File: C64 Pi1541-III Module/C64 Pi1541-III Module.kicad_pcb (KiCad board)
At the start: 2 copper layers, 100 x 100 mm, 25 parts, among them J1 DC IN, J2 C64_IEC, J3 C64_IEC, J8 Module_Panel, M1 Mounting, M2 Mounting, M3 Mounting, M4 Mounting, U1 7406

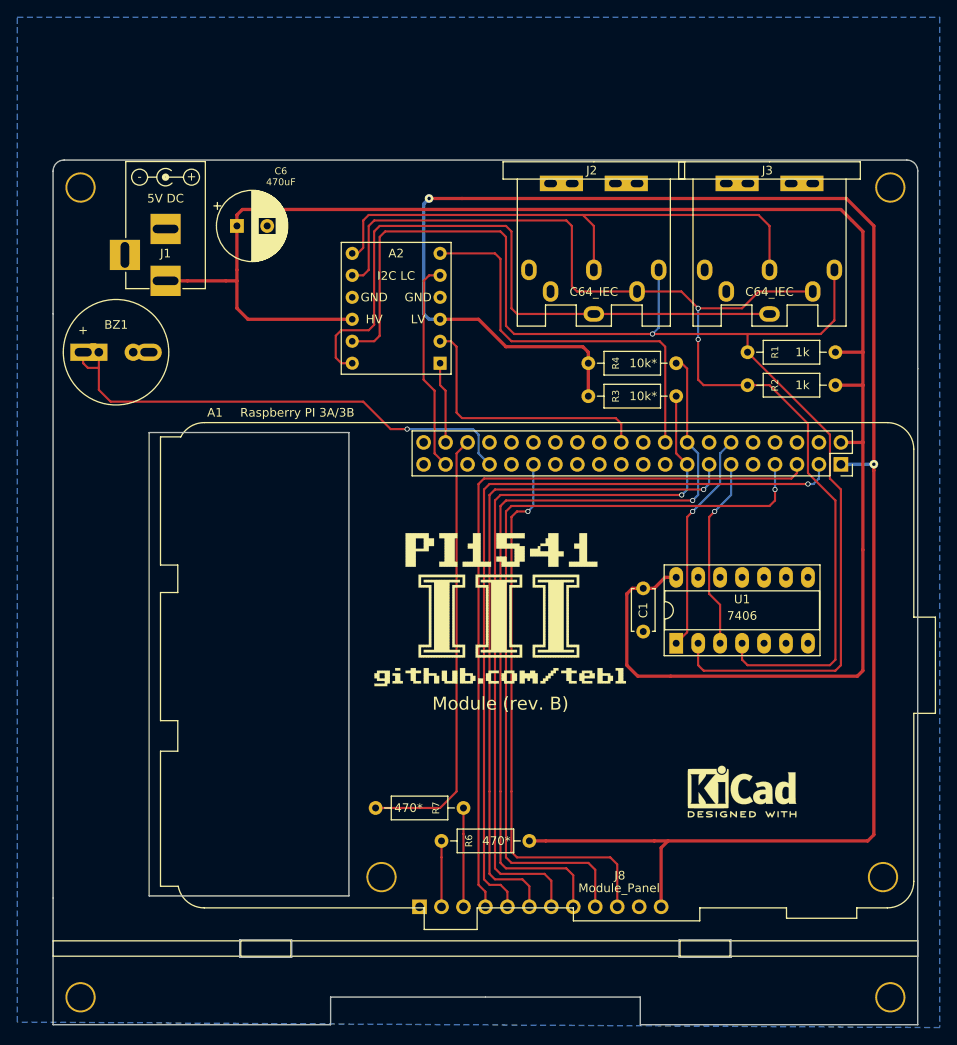
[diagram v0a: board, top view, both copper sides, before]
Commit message: Moved components around to make it easier to build
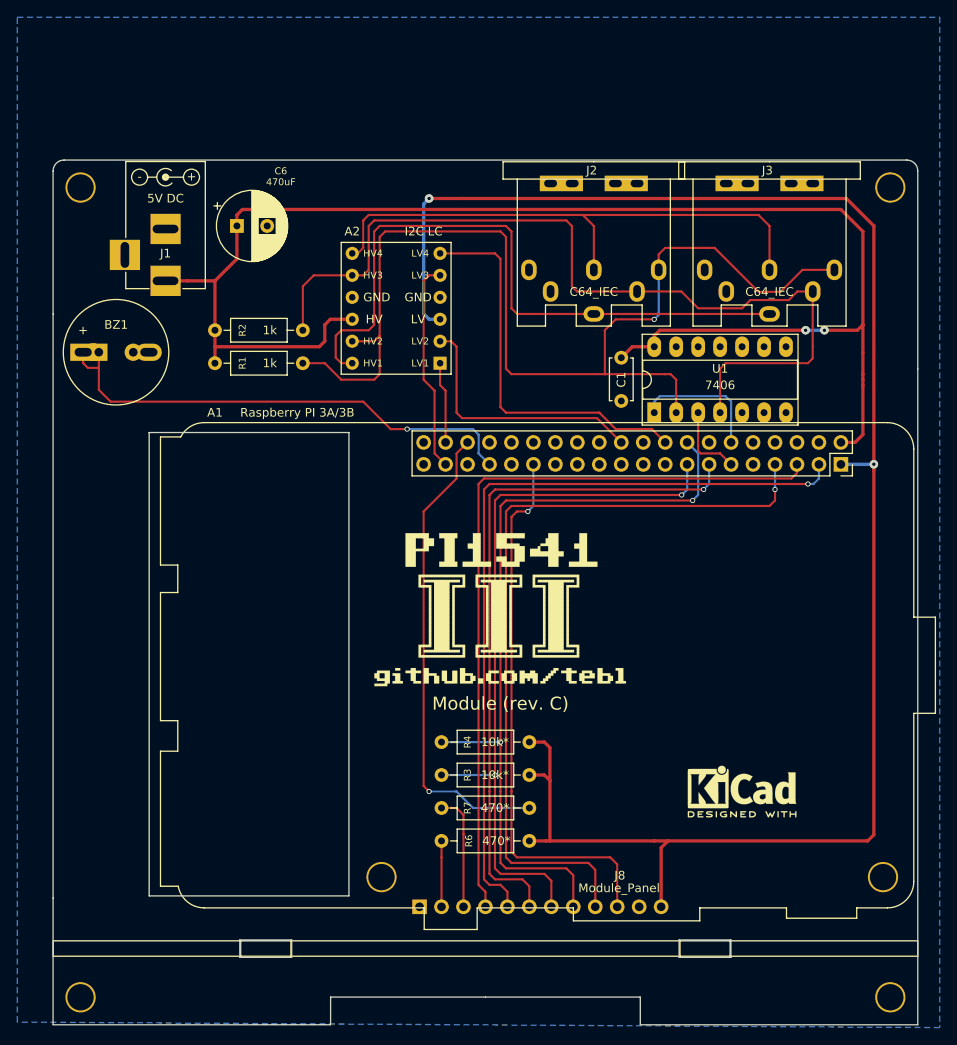
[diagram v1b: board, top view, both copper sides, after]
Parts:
- moved R2 72.0 mm to (88.9, 74.3), turned to 0 degrees
- moved R1 71.8 mm to (88.9, 78.1), turned to 0 degrees
- moved R3 44.3 mm to (125.3, 125.7), turned to 180 degrees
- moved R4 44.3 mm to (125.3, 121.9), turned to 180 degrees
- moved C1 26.8 mm to (135.9, 77.5)
- moved U1 26.8 mm to (139.7, 83.8)
- moved REF*** 10.4 mm to (149.9, 127.0)
- moved R7 7.62 mm to (125.3, 129.5)
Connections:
- R7 pad 1: LED_ACT -> RPI_LED
- R7 pad 2: RPI_LED -> LED_ACT
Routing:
- net +5V: track 209.2 -> 172.6 mm, vias 0 -> 2
- net C64_CLK: track 132.9 -> 103.3 mm, vias 2 -> 0
- net C64_DATA: track 155.2 -> 126.5 mm
- net RPI_CLK_OUT: track 22.3 -> 8.89 mm, vias 1 -> 0
- net RPI_DATA_OUT: track 25.9 -> 15.4 mm, vias 1 -> 0
- net +3V3: track 214.6 -> 206.9 mm
- net RPI_LED: track 51.0 -> 55.1 mm, vias 0 -> 1
- net SW3_DOWN: track 94.0 -> 90.7 mm, vias 1 -> 2
- net SW2_UP: track 86.7 -> 84.5 mm, vias 1 -> 2
- net LED_ACT: track 11.4 -> 13.5 mm
- net RPI_ATN: track 46.4 -> 45.1 mm
- net RPI_DATA_IN: track 31.5 -> 30.3 mm
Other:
- board text added: "Module (rev. C)"
- board text removed: "Module (rev. B)"
